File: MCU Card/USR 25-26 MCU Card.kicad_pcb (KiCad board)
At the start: 2 copper layers, 129.5 x 76.8 mm, 10 parts

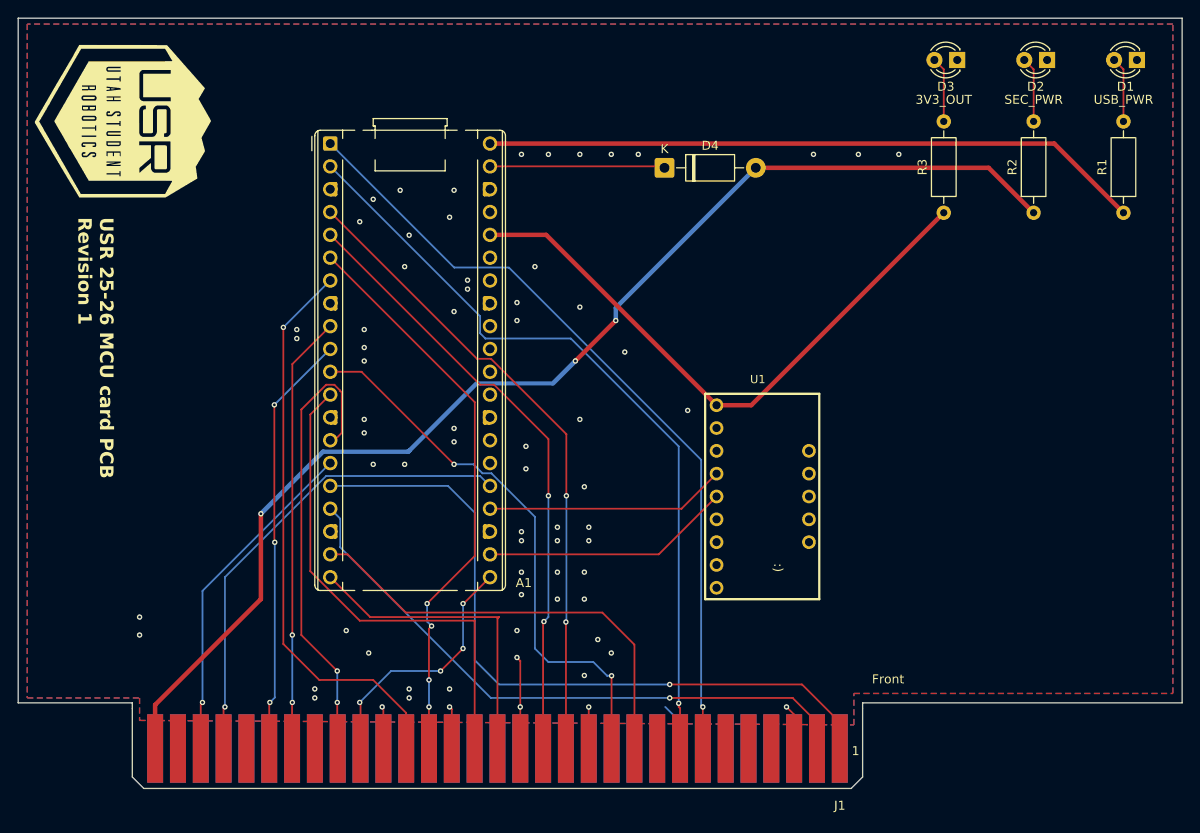
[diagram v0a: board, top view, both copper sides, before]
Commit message: Finalized designs for MCU card, Analog board, and MDCB
Added additional vias to all in order to minimize ground loops and stitch together front and back ground planes.
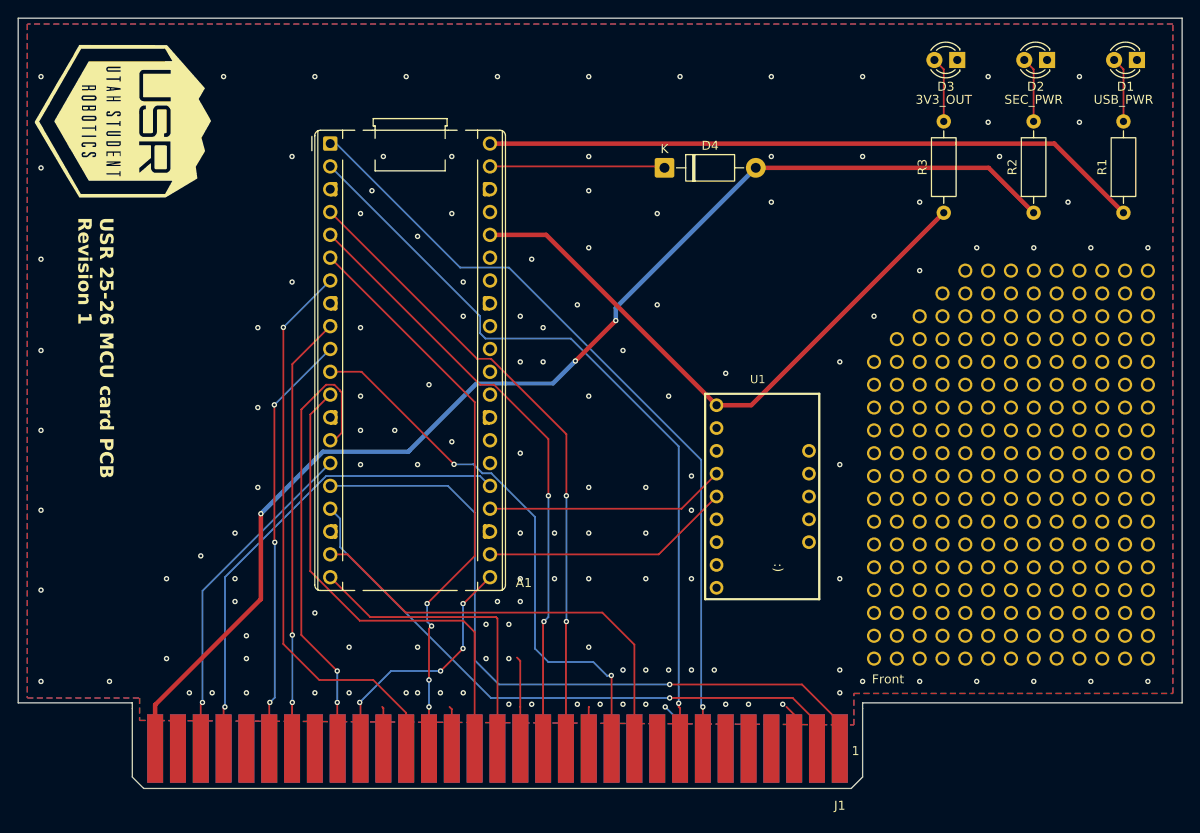
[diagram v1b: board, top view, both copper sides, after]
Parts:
- added ?: , , F.Cu at (152.4, 119.4)
- added ?: , , F.Cu at (152.4, 99.1)
- added ?: , , F.Cu at (165.1, 134.6)
- added ?: , , F.Cu at (167.6, 109.2)
- added ?: , , F.Cu at (152.4, 132.1)
- added ?: , , F.Cu at (165.1, 91.4)
- added ?: , , F.Cu at (172.7, 101.6)
- added ?: , , F.Cu at (162.6, 101.6)
- added ?: , , F.Cu at (165.1, 127.0)
- added ?: , , F.Cu at (142.2, 114.3)
- added ?: , , F.Cu at (170.2, 129.5)
- added ?: , , F.Cu at (144.8, 121.9)
- added ?: , , F.Cu at (152.4, 101.6)
- added ?: , , F.Cu at (149.9, 134.6)
- added ?: , , F.Cu at (172.7, 99.1)
- added ?: , , F.Cu at (152.4, 94.0)
- added ?: , , F.Cu at (162.6, 121.9)
- added ?: , , F.Cu at (172.7, 129.5)
- added ?: , , F.Cu at (172.7, 94.0)
- added ?: , , F.Cu at (172.7, 91.4)
- added ?: , , F.Cu at (172.7, 132.1)
- added ?: , , F.Cu at (162.6, 119.4)
- added ?: , , F.Cu at (170.2, 121.9)
- added ?: , , F.Cu at (165.1, 119.4)
- added ?: , , F.Cu at (144.8, 109.2)
- added ?: , , F.Cu at (142.2, 119.4)
- added ?: , , F.Cu at (172.7, 116.8)
- added ?: , , F.Cu at (147.3, 132.1)
- added ?: , , F.Cu at (172.7, 111.8)
- added ?: , , F.Cu at (165.1, 124.5)
- added ?: , , F.Cu at (154.9, 111.8)
- added ?: , , F.Cu at (157.5, 104.1)
- added ?: , , F.Cu at (170.2, 127.0)
- added ?: , , F.Cu at (147.3, 109.2)
- added ?: , , F.Cu at (157.5, 124.5)
- added ?: , , F.Cu at (170.2, 94.0)
- added ?: , , F.Cu at (167.6, 104.1)
- added ?: , , F.Cu at (165.1, 94.0)
- added ?: , , F.Cu at (162.6, 96.5)
- added ?: , , F.Cu at (157.5, 134.6)
- added ?: , , F.Cu at (149.9, 96.5)
- added ?: , , F.Cu at (152.4, 106.7)
- added ?: , , F.Cu at (154.9, 124.5)
- added ?: , , F.Cu at (167.6, 99.1)
- added ?: , , F.Cu at (167.6, 116.8)
- added ?: , , F.Cu at (154.9, 99.1)
- added ?: , , F.Cu at (142.2, 111.8)
- added ?: , , F.Cu at (154.9, 94.0)
- added ?: , , F.Cu at (160.0, 121.9)
- added ?: , , F.Cu at (167.6, 127.0)
- added ?: , , F.Cu at (152.4, 116.8)
- added ?: , , F.Cu at (157.5, 109.2)
- added ?: , , F.Cu at (154.9, 127.0)
- added ?: , , F.Cu at (154.9, 121.9)
- added ?: , , F.Cu at (172.7, 124.5)
- added ?: , , F.Cu at (167.6, 96.5)
- added ?: , , F.Cu at (170.2, 101.6)
- added ?: , , F.Cu at (144.8, 106.7)
- added ?: , , F.Cu at (170.2, 114.3)
- added ?: , , F.Cu at (162.6, 91.4)
- added ?: , , F.Cu at (144.8, 127.0)
- added ?: , , F.Cu at (165.1, 121.9)
- added ?: , , F.Cu at (157.5, 129.5)
- added ?: , , F.Cu at (160.0, 134.6)
- added ?: , , F.Cu at (142.2, 124.5)
- added ?: , , F.Cu at (167.6, 124.5)
- added ?: , , F.Cu at (167.6, 106.7)
- added ?: , , F.Cu at (147.3, 104.1)
- added ?: , , F.Cu at (149.9, 101.6)
- added ?: , , F.Cu at (157.5, 116.8)
- added ?: , , F.Cu at (144.8, 132.1)
- added ?: , , F.Cu at (170.2, 91.4)
- added ?: , , F.Cu at (144.8, 129.5)
- added ?: , , F.Cu at (142.2, 109.2)
- added ?: , , F.Cu at (165.1, 99.1)
- added ?: , , F.Cu at (154.9, 96.5)
- added ?: , , F.Cu at (149.9, 106.7)
- added ?: , , F.Cu at (149.9, 132.1)
- added ?: , , F.Cu at (167.6, 94.0)
- added ?: , , F.Cu at (172.7, 119.4)
- added ?: , , F.Cu at (162.6, 104.1)
- added ?: , , F.Cu at (142.2, 127.0)
- added ?: , , F.Cu at (167.6, 119.4)
- added ?: , , F.Cu at (147.3, 96.5)
- added ?: , , F.Cu at (152.4, 91.4)
- added ?: , , F.Cu at (160.0, 99.1)
- added ?: , , F.Cu at (160.0, 119.4)
- added ?: , , F.Cu at (162.6, 124.5)
- added ?: , , F.Cu at (144.8, 134.6)
- added ?: , , F.Cu at (170.2, 111.8)
- added ?: , , F.Cu at (147.3, 121.9)
- added ?: , , F.Cu at (167.6, 121.9)
- added ?: , , F.Cu at (165.1, 129.5)
- added ?: , , F.Cu at (167.6, 91.4)
- added ?: , , F.Cu at (154.9, 114.3)
- added ?: , , F.Cu at (157.5, 94.0)
- added ?: , , F.Cu at (172.7, 106.7)
- added ?: , , F.Cu at (165.1, 116.8)
- added ?: , , F.Cu at (172.7, 114.3)
- added ?: , , F.Cu at (157.5, 111.8)
- added ?: , , F.Cu at (152.4, 124.5)
- added ?: , , F.Cu at (152.4, 134.6)
- added ?: , , F.Cu at (149.9, 94.0)
- added ?: , , F.Cu at (157.5, 106.7)
- added ?: , , F.Cu at (149.9, 99.1)
- added ?: , , F.Cu at (144.8, 111.8)
- added ?: , , F.Cu at (152.4, 121.9)
- added ?: , , F.Cu at (142.2, 106.7)
- added ?: , , F.Cu at (157.5, 121.9)
- added ?: , , F.Cu at (144.8, 99.1)
- added ?: , , F.Cu at (162.6, 116.8)
- added ?: , , F.Cu at (144.8, 124.5)
- added ?: , , F.Cu at (162.6, 132.1)
- added ?: , , F.Cu at (160.0, 124.5)
- added ?: , , F.Cu at (160.0, 104.1)
- added ?: , , F.Cu at (157.5, 119.4)
- added ?: , , F.Cu at (144.8, 104.1)
- added ?: , , F.Cu at (149.9, 114.3)
- added ?: , , F.Cu at (149.9, 116.8)
- added ?: , , F.Cu at (154.9, 106.7)
- added ?: , , F.Cu at (157.5, 101.6)
- added ?: , , F.Cu at (147.3, 106.7)
- added ?: , , F.Cu at (154.9, 132.1)
- added ?: , , F.Cu at (160.0, 106.7)
- added ?: , , F.Cu at (144.8, 119.4)
- added ?: , , F.Cu at (142.2, 132.1)
- added ?: , , F.Cu at (154.9, 101.6)
- added ?: , , F.Cu at (152.4, 129.5)
- added ?: , , F.Cu at (152.4, 127.0)
- added ?: , , F.Cu at (165.1, 114.3)
- added ?: , , F.Cu at (147.3, 119.4)
- added ?: , , F.Cu at (160.0, 132.1)
- added ?: , , F.Cu at (154.9, 116.8)
- added ?: , , F.Cu at (172.7, 104.1)
- added ?: , , F.Cu at (162.6, 109.2)
- added ?: , , F.Cu at (170.2, 134.6)
- added ?: , , F.Cu at (152.4, 104.1)
- added ?: , , F.Cu at (147.3, 99.1)
- added ?: , , F.Cu at (160.0, 91.4)
- added ?: , , F.Cu at (165.1, 96.5)
- added ?: , , F.Cu at (152.4, 111.8)
- added ?: , , F.Cu at (149.9, 119.4)
- added ?: , , F.Cu at (154.9, 129.5)
- added ?: , , F.Cu at (160.0, 116.8)
- added ?: , , F.Cu at (172.7, 134.6)
- added ?: , , F.Cu at (170.2, 96.5)
- added ?: , , F.Cu at (142.2, 104.1)
- added ?: , , F.Cu at (167.6, 134.6)
- added ?: , , F.Cu at (167.6, 132.1)
- added ?: , , F.Cu at (157.5, 114.3)
- added ?: , , F.Cu at (165.1, 132.1)
- added ?: , , F.Cu at (157.5, 132.1)
- added ?: , , F.Cu at (172.7, 127.0)
- added ?: , , F.Cu at (154.9, 134.6)
- added ?: , , F.Cu at (157.5, 91.4)
- added ?: , , F.Cu at (172.7, 121.9)
- added ?: , , F.Cu at (167.6, 114.3)
- added ?: , , F.Cu at (147.3, 116.8)
- added ?: , , F.Cu at (142.2, 134.6)
- added ?: , , F.Cu at (149.9, 124.5)
- added ?: , , F.Cu at (170.2, 116.8)
- added ?: , , F.Cu at (160.0, 114.3)
- added ?: , , F.Cu at (160.0, 94.0)
- added ?: , , F.Cu at (147.3, 124.5)
- added ?: , , F.Cu at (162.6, 114.3)
- added ?: , , F.Cu at (154.9, 91.4)
- added ?: , , F.Cu at (147.3, 114.3)
- added ?: , , F.Cu at (162.6, 127.0)
- added ?: , , F.Cu at (149.9, 111.8)
- added ?: , , F.Cu at (152.4, 109.2)
- added ?: , , F.Cu at (152.4, 96.5)
- added ?: , , F.Cu at (172.7, 96.5)
- added ?: , , F.Cu at (165.1, 104.1)
- added ?: , , F.Cu at (170.2, 109.2)
- added ?: , , F.Cu at (154.9, 104.1)
- added ?: , , F.Cu at (160.0, 127.0)
- added ?: , , F.Cu at (147.3, 101.6)
- added ?: , , F.Cu at (167.6, 129.5)
- added ?: , , F.Cu at (160.0, 129.5)
- added ?: , , F.Cu at (170.2, 132.1)
- added ?: , , F.Cu at (157.5, 96.5)
- added ?: , , F.Cu at (160.0, 111.8)
- added ?: , , F.Cu at (147.3, 127.0)
- added ?: , , F.Cu at (170.2, 104.1)
- added ?: , , F.Cu at (142.2, 121.9)
- added ?: , , F.Cu at (144.8, 101.6)
- added ?: , , F.Cu at (170.2, 119.4)
- added ?: , , F.Cu at (152.4, 114.3)
- added ?: , , F.Cu at (167.6, 111.8)
- added ?: , , F.Cu at (162.6, 106.7)
- added ?: , , F.Cu at (165.1, 109.2)
- added ?: , , F.Cu at (157.5, 99.1)
- added ?: , , F.Cu at (142.2, 116.8)
- added ?: , , F.Cu at (162.6, 99.1)
- added ?: , , F.Cu at (162.6, 129.5)
- added ?: , , F.Cu at (142.2, 101.6)
- added ?: , , F.Cu at (149.9, 109.2)
- added ?: , , F.Cu at (160.0, 109.2)
- added ?: , , F.Cu at (165.1, 111.8)
- added ?: , , F.Cu at (157.5, 127.0)
- added ?: , , F.Cu at (147.3, 129.5)
- added ?: , , F.Cu at (165.1, 106.7)
- added ?: , , F.Cu at (149.9, 129.5)
- added ?: , , F.Cu at (170.2, 99.1)
- added ?: , , F.Cu at (142.2, 129.5)
- added ?: , , F.Cu at (144.8, 114.3)
- added ?: , , F.Cu at (170.2, 124.5)
- added ?: , , F.Cu at (147.3, 134.6)
- added ?: , , F.Cu at (170.2, 106.7)
- added ?: , , F.Cu at (160.0, 96.5)
- added ?: , , F.Cu at (147.3, 111.8)
- added ?: , , F.Cu at (154.9, 119.4)
- added ?: , , F.Cu at (144.8, 116.8)
- added ?: , , F.Cu at (160.0, 101.6)
- added ?: , , F.Cu at (162.6, 111.8)
- added ?: , , F.Cu at (149.9, 121.9)
- added ?: , , F.Cu at (149.9, 127.0)
- added ?: , , F.Cu at (154.9, 109.2)
- added ?: , , F.Cu at (167.6, 101.6)
- added ?: , , F.Cu at (162.6, 134.6)
- added ?: , , F.Cu at (165.1, 101.6)
- added ?: , , F.Cu at (172.7, 109.2)
- added ?: , , F.Cu at (149.9, 104.1)
- added ?: , , F.Cu at (162.6, 94.0)
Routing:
- net /M2_SLP: track 55.4 -> 54.6 mm
- net GND: vias 70 -> 137

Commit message: Modify names on silkscreen
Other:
- board text added: "Peter Burt Vincent Banh MCU Card 25-26"
- board text removed: "Peter Burt JG Vincent Banh MCU Card 25-26"
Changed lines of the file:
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@@
 		(capping no)
 		(filling no)
-		(zone_defaults)
 		(pcbplotparams
 			(layerselection 0x00000000_00000000_55555555_5755f5ff)
@@
 		)
 	)
-	(gr_text "Peter Burt\nJG\nVincent Banh\nMCU Card 25-26"
+	(gr_text "Peter Burt\nVincent Banh\nMCU Card 25-26"
 		(at 48.26 138.43 0)
 		(layer "B.SilkS")
@@
 			(keep_text_aligned yes)
 		)
-		(gr_text "76.2"
+		(gr_text "3000"
 			(at 188.35 101.4475 90)
 			(layer "Cmts.User")
@@
 			(keep_text_aligned yes)
 		)
-		(gr_text "129.54"
+		(gr_text "5100"
 			(at 111.76 50.35 0)
 			(layer "Cmts.User")
